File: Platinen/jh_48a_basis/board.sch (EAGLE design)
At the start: 29 parts, among them X1 14867

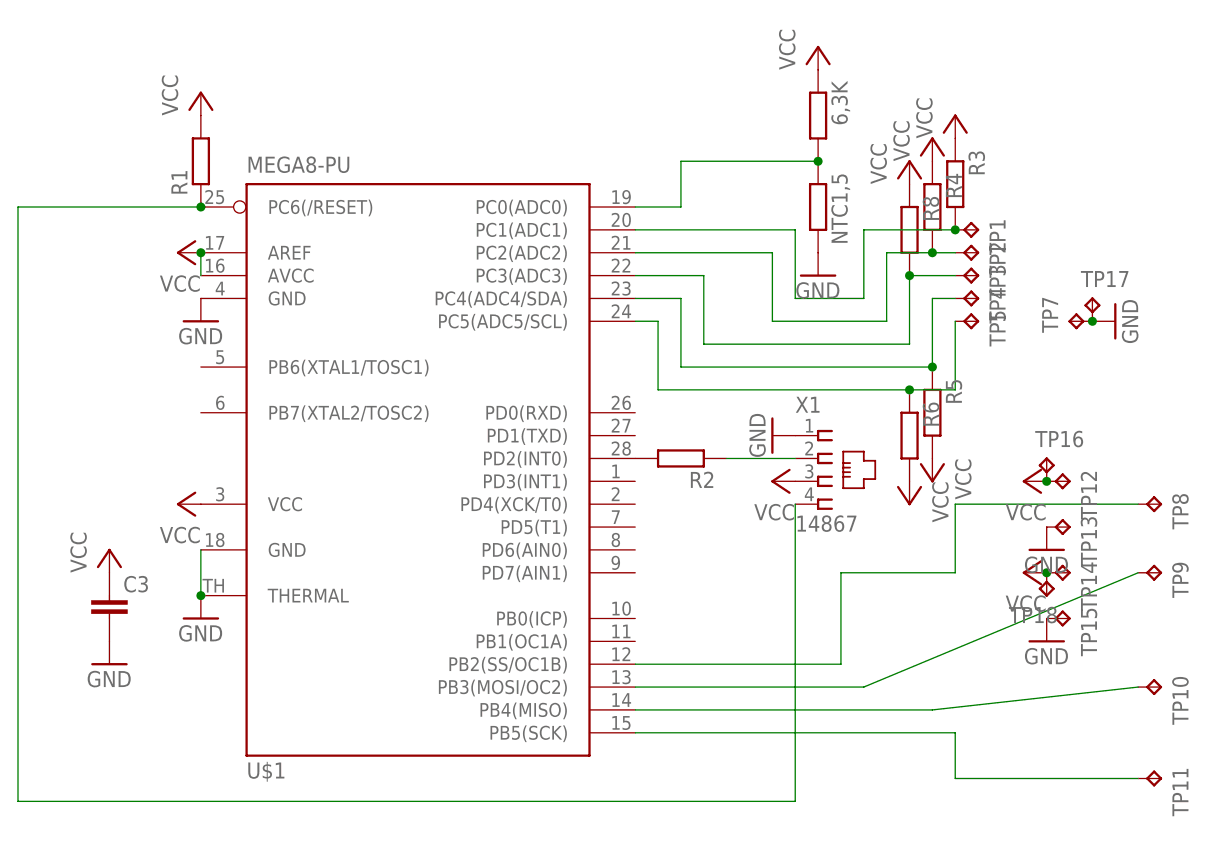
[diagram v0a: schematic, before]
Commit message: layout: update with C
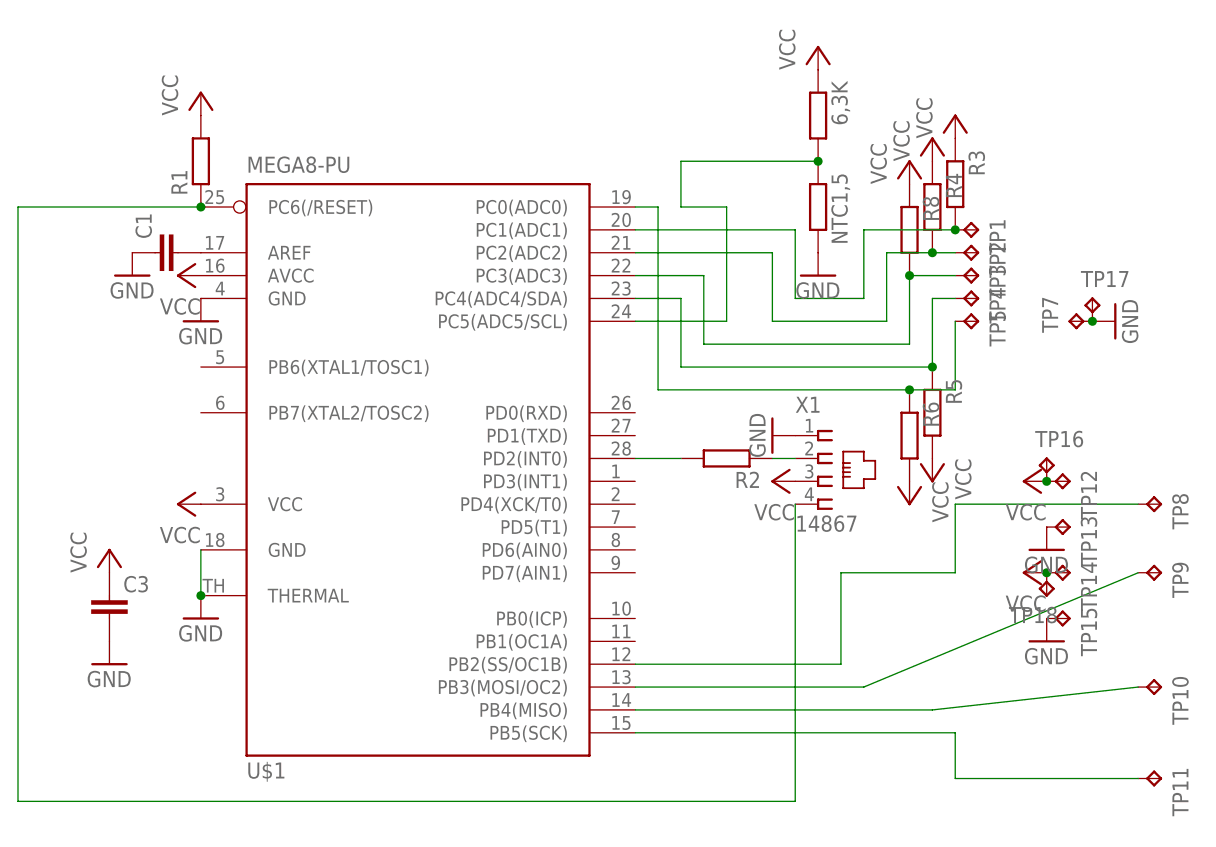
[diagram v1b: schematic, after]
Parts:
- added C1: (no value), rcl:C-EUC0805
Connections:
- removed net N$2: 6,3K.2, NTC1,5.1, U$1.PC0(ADC0)
- new net N$18: 6,3K.2, NTC1,5.1, U$1.PC5(ADC5/SCL)
- new net N$6: C1.2, U$1.AREF
- net GND: now also C1.1
- net N$17: now also U$1.PC0(ADC0); no longer U$1.PC5(ADC5/SCL)
- net VCC: no longer U$1.AREF
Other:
- moved on the sheet: R2
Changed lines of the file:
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@@
 <?xml version="1.0" encoding="utf-8"?>
 <!DOCTYPE eagle SYSTEM "eagle.dtd">
-<eagle version="6.3">
+<eagle version="6.2">
 <drawing>
 <settings>
@@
 </variantdefs>
 <classes>
-<class number="0" name="default" width="0" drill="0">
+<class number="0" name="default" width="0.12" drill="0">
 </class>
 </classes>
@@
 <attribute name="TP_SIGNAL_NAME" value=""/>
 </part>
+<part name="GND6" library="supply1" deviceset="GND" device=""/>
+<part name="C1" library="rcl" deviceset="C-EU" device="C0805"/>
 </parts>
 <sheets>
@@
 <instance part="GND2" gate="1" x="10.16" y="27.94"/>
 <instance part="P+1" gate="VCC" x="7.62" y="40.64" rot="R90"/>
-<instance part="P+2" gate="VCC" x="7.62" y="68.58" rot="R90"/>
+<instance part="P+2" gate="VCC" x="7.62" y="66.04" rot="R90"/>
 <instance part="GND4" gate="1" x="10.16" y="60.96"/>
 <instance part="R1" gate="G$1" x="10.16" y="78.74" rot="R90"/>
@@
 <instance part="GND3" gate="1" x="0" y="22.86"/>
 <instance part="C3" gate="G$1" x="0" y="30.48"/>
-<instance part="R2" gate="G$1" x="63.5" y="45.72" rot="R180"/>
+<instance part="R2" gate="G$1" x="68.58" y="45.72" rot="R180"/>
 <instance part="6,3K" gate="G$1" x="78.74" y="83.82" rot="R270"/>
 <instance part="NTC1,5" gate="G$1" x="78.74" y="73.66" rot="R270"/>
@@
 <instance part="TP17" gate="G$1" x="109.22" y="63.5"/>
 <instance part="TP18" gate="G$1" x="104.14" y="30.48" rot="R180"/>
+<instance part="GND6" gate="1" x="2.54" y="66.04"/>
+<instance part="C1" gate="G$1" x="5.08" y="68.58" rot="R90"/>
 </instances>
 <busses>
@@
 <pinref part="TP15" gate="G$1" pin="TP"/>
 </segment>
+<segment>
+<pinref part="C1" gate="G$1" pin="1"/>
+<pinref part="GND6" gate="1" pin="GND"/>
+</segment>
 </net>
 <net name="VCC" class="0">
@@
 </segment>
 <segment>
-<wire x1="10.16" y1="66.04" x2="10.16" y2="68.58" width="0.1524" layer="91"/>
-<junction x="10.16" y="68.58"/>
-<pinref part="U$1" gate="G$1" pin="AREF"/>
 <pinref part="P+2" gate="VCC" pin="VCC"/>
 <pinref part="U$1" gate="G$1" pin="AVCC"/>
@@
 <pinref part="U$1" gate="G$1" pin="PD2(INT0)"/>
 <pinref part="R2" gate="G$1" pin="2"/>
-</segment>
-</net>
-<net name="N$2" class="0">
-<segment>
-<pinref part="6,3K" gate="G$1" pin="2"/>
-<pinref part="NTC1,5" gate="G$1" pin="1"/>
-<wire x1="78.74" y1="78.74" x2="63.5" y2="78.74" width="0.1524" layer="91"/>
-<wire x1="63.5" y1="78.74" x2="63.5" y2="73.66" width="0.1524" layer="91"/>
-<junction x="78.74" y="78.74"/>
-<pinref part="U$1" gate="G$1" pin="PC0(ADC0)"/>
-<wire x1="58.42" y1="73.66" x2="63.5" y2="73.66" width="0.1524" layer="91"/>
+<wire x1="63.5" y1="45.72" x2="58.42" y2="45.72" width="0.1524" layer="91"/>
 </segment>
 </net>
@@
 </segment>
 </net>
-<net name="N$13" class="0">
+<net name="N$51" class="0">
 <segment>
 <wire x1="58.42" y1="68.58" x2="73.66" y2="68.58" width="0.1524" layer="91"/>
@@
 <net name="N$17" class="0">
 <segment>
-<pinref part="U$1" gate="G$1" pin="PC5(ADC5/SCL)"/>
-<wire x1="58.42" y1="60.96" x2="60.96" y2="60.96" width="0.1524" layer="91"/>
-<wire x1="60.96" y1="60.96" x2="60.96" y2="53.34" width="0.1524" layer="91"/>
 <wire x1="60.96" y1="53.34" x2="88.9" y2="53.34" width="0.1524" layer="91"/>
 <wire x1="88.9" y1="53.34" x2="93.98" y2="53.34" width="0.1524" layer="91"/>
@@
 <junction x="88.9" y="53.34"/>
 <pinref part="TP5" gate="G$1" pin="TP"/>
+<wire x1="60.96" y1="53.34" x2="60.96" y2="73.66" width="0.1524" layer="91"/>
+<pinref part="U$1" gate="G$1" pin="PC0(ADC0)"/>
+<wire x1="60.96" y1="73.66" x2="58.42" y2="73.66" width="0.1524" layer="91"/>
 </segment>
 </net>
@@
 <pinref part="X1" gate="G$1" pin="2"/>
 <pinref part="R2" gate="G$1" pin="1"/>
-<wire x1="76.2" y1="45.72" x2="68.58" y2="45.72" width="0.1524" layer="91"/>
+<wire x1="76.2" y1="45.72" x2="73.66" y2="45.72" width="0.1524" layer="91"/>
 </segment>
 </net>
@@
 </segment>
 </net>
+<net name="N$6" class="0">
+<segment>
+<pinref part="U$1" gate="G$1" pin="AREF"/>
+<pinref part="C1" gate="G$1" pin="2"/>
+</segment>
+</net>
+<net name="N$18" class="0">
+<segment>
+<pinref part="U$1" gate="G$1" pin="PC5(ADC5/SCL)"/>
+<wire x1="58.42" y1="60.96" x2="68.58" y2="60.96" width="0.1524" layer="91"/>
+<wire x1="68.58" y1="60.96" x2="68.58" y2="73.66" width="0.1524" layer="91"/>
+<pinref part="6,3K" gate="G$1" pin="2"/>
+<pinref part="NTC1,5" gate="G$1" pin="1"/>
+<wire x1="78.74" y1="78.74" x2="63.5" y2="78.74" width="0.1524" layer="91"/>
+<wire x1="63.5" y1="78.74" x2="63.5" y2="73.66" width="0.1524" layer="91"/>
+<junction x="78.74" y="78.74"/>
+<wire x1="68.58" y1="73.66" x2="63.5" y2="73.66" width="0.1524" layer="91"/>
+</segment>
+</net>
